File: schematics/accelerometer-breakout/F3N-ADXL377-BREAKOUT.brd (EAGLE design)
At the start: 60.6 x 29.2 mm, 8 parts

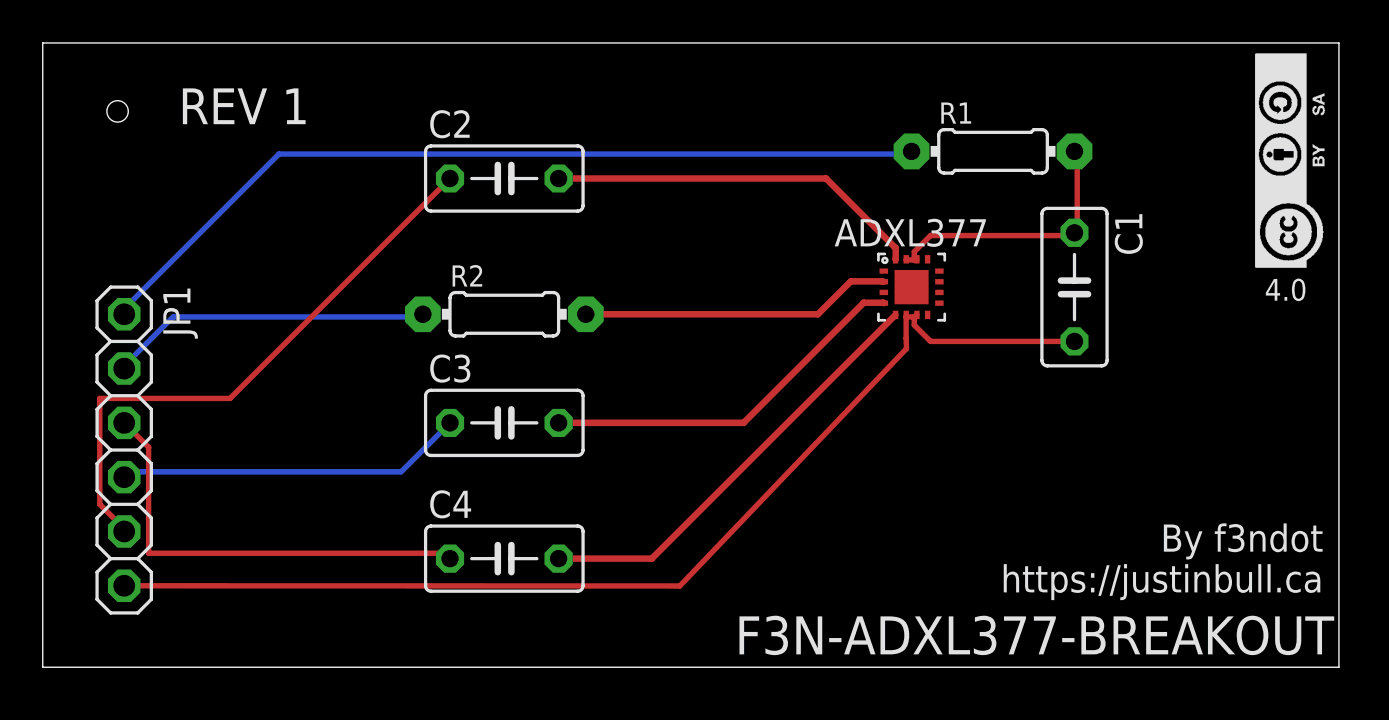
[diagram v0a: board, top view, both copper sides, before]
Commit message: Routed, t/b GND plane, Cap parallel fix
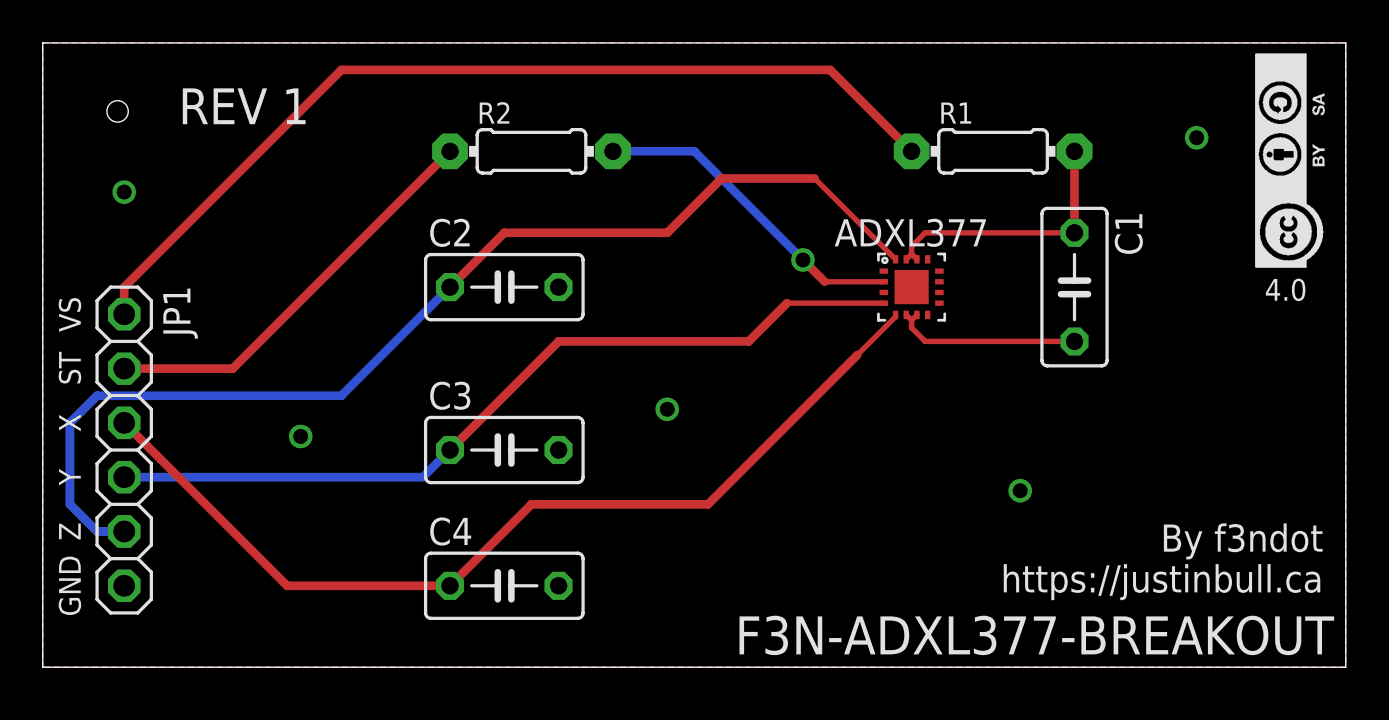
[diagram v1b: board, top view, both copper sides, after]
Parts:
- moved R2 7.73 mm to (22.9, 24.1)
- moved C2 5.08 mm to (21.6, 17.8)
- moved C4 1.27 mm to (21.6, 3.81)
- moved C3 1.27 mm to (21.6, 10.2)
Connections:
- net N$3 renamed VS
- net N$5 renamed ST
- removed net N$10: ADXL377.P$4, C3.2
- removed net N$11: ADXL377.P$5, C4.2
- removed net N$2: C4.1, JP1.3
- removed net N$6: C3.1, JP1.4
- removed net N$7: C2.1, JP1.5
- removed net N$8: ADXL377.P$16, C2.2
- new net X: ADXL377.P$5, C4.1, JP1.3
- new net Y: ADXL377.P$4, C3.1, JP1.4
- new net Z: ADXL377.P$16, C2.1, JP1.5
- net GND: now also C2.2, C3.2, C4.2
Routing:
- net Z: track 0.00 -> 51.8 mm
- net X: track 0.00 -> 44.5 mm
- net GND: track 51.6 -> 8.95 mm, vias 0 -> 5
- net Y: track 0.00 -> 38.9 mm
- net N$7: track 27.3 -> 0.00 mm
- net N$2: track 20.9 -> 0.00 mm
- net N$11: track 20.5 -> 0.00 mm
- net N$8: track 17.6 -> 0.00 mm
- net N$10: track 17.5 -> 0.00 mm
- net N$6: track 16.4 -> 0.00 mm
- net ST: track 15.1 -> 19.4 mm
- net VS: track 40.1 -> 43.9 mm
- net N$9: track 14.6 -> 15.2 mm, vias 0 -> 1
- added copper zone on layer 1, net GND
- added copper zone on layer 16, net GND
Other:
- board size 60.6 x 29.2 mm -> 60.9 x 29.2 mm
- board text added: "GND"
- board text added: "ST"
- board text added: "VS"
- board text added: "X"
- board text added: "Y"
- board text added: "Z"
